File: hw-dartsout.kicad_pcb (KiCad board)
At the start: 2 copper layers, 45 parts, among them J1 Conn_01x10_Socket, J2 Conn_01x10_Socket, J3 Conn_01x02_Pin, J4 Conn_01x04_Pin, SW1 SW_Push, U1 ESP32-S3-WROOM-1, U3 NCP1117-3.3_SOT223

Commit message: PCB routed
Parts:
- removed TP2, TP3: TestPoint, TestPoint:TestPoint_Pad_D1.5mm
- added J5: Conn_01x10_Socket, Connector_PinSocket_2.54mm:PinSocket_1x10_P2.54mm_Vertical, F.Cu at (174.2, 118.6)
- added J6: Conn_01x10_Socket, Connector_PinSocket_2.54mm:PinSocket_1x10_P2.54mm_Vertical, F.Cu at (174.2, 103.5)
- added TP6: TestPoint, TestPoint:TestPoint_Pad_D1.5mm, F.Cu at (87.3, 96.8)
- H1, H2, H3, H4: footprint MountingHole:MountingHole_3.2mm_M3_Pad_TopBottom -> MountingHole:MountingHole_3.2mm_M3_DIN965_Pad_TopBottom
- U1: value ESP32-S3-WROOM-1 -> ESP32-S2-SOLO; footprint PCM_Espressif:ESP32-S3-WROOM-1 -> PCM_Espressif:ESP32-S2-SOLO
- moved H2 24.8 mm to (174.0, 98.1)
- moved H4 24.2 mm to (174.0, 126.9)
- moved JP1 15.8 mm to (164.4, 127.2), turned to 0 degrees
- moved JP2 14.5 mm to (153.8, 127.1), turned to 180 degrees
- moved TP4 8.96 mm to (94.9, 96.8), turned to 180 degrees
- moved TP5 7.72 mm to (98.7, 96.8), turned to 180 degrees
- moved TP1 5.16 mm to (91.1, 96.8), turned to 180 degrees
- moved H1 2.86 mm to (80.2, 98.1)
- moved H3 2.10 mm to (80.2, 126.9)
- moved J3 0.55 mm to (80.3, 110.1)
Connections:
- TP1 pad 1: Net-(U1-SPIIO6/GPIO35/FSPID/SUBSPID) -> Net-(U1-GPIO1/TOUCH1/ADC1_CH0)
- TP4 pad 1: Net-(U1-GPIO45) -> Net-(U1-GPIO2/TOUCH2/ADC1_CH1)
- U1 pad 10: /COL_05 -> /ROW_06
- U1 pad 11: /COL_06 -> /ROW_05
- U1 pad 12: /ROW_08 -> /ROW_04
- U1 pad 17: /ROW_09 -> /ROW_02
- U1 pad 18: /ROW_10 -> /ROW_01
- U1 pad 19: /COL_01 -> /COL_10
- U1 pad 20: /COL_02 -> /COL_09
- U1 pad 21: /COL_03 -> /COL_08
- U1 pad 22: /COL_04 -> /COL_07
- U1 pad 23: /COL_07 -> /COL_06
- U1 pad 24: /COL_09 -> /COL_05
- U1 pad 25: /COL_10 -> /COL_04
- U1 pad 26: Net-(U1-GPIO45) -> unconnected-(U1-GPIO45-Pad26)
- U1 pad 28: Net-(U1-SPIIO6/GPIO35/FSPID/SUBSPID) -> /COL_03
- U1 pad 29: Net-(U1-SPIIO7/GPIO36/FSPICLK/SUBSPICLK) -> /COL_02
- U1 pad 30: Net-(U1-SPIDQS/GPIO37/FSPIQ/SUBSPIQ) -> /COL_01
- U1 pad 31: /COL_08 -> Net-(U1-GPIO38/FSPIWP)
- U1 pad 38: /ROW_02 -> Net-(U1-GPIO2/TOUCH2/ADC1_CH1)
- U1 pad 39: /ROW_01 -> Net-(U1-GPIO1/TOUCH1/ADC1_CH0)
- U1 pad 4: /ROW_04 -> /ROW_10
- U1 pad 5: /ROW_05 -> /ROW_09
- U1 pad 6: /ROW_06 -> /ROW_08
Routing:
- net +3V3: track 0.00 -> 131.8 mm, vias 0 -> 2
- net /COL_03: track 31.5 -> 94.4 mm, vias 0 -> 3
- net /COL_02: track 34.0 -> 96.7 mm, vias 0 -> 3
- net /COL_01: track 36.6 -> 99.0 mm, vias 0 -> 3
- net /COL_04: track 28.9 -> 86.5 mm, vias 0 -> 1
- net /ROW_01: track 35.4 -> 91.6 mm
- net /ROW_02: track 31.6 -> 87.4 mm
- net /COL_05: track 26.4 -> 82.1 mm, vias 0 -> 1
- net /COL_06: track 23.9 -> 78.0 mm, vias 0 -> 1
- net /COL_07: track 21.3 -> 73.8 mm, vias 0 -> 1
- net /ROW_03: track 29.0 -> 80.7 mm
- net /COL_08: track 18.8 -> 69.6 mm, vias 0 -> 1
- net /COL_09: track 16.2 -> 65.4 mm, vias 0 -> 1
- net /ROW_04: track 27.0 -> 73.3 mm
- net /ROW_10: track 15.5 -> 60.8 mm
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- added copper zone on B.Cu, net GND
- added copper zone on F.Cu, net GND
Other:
- board outline added: 100 x 35 mm
- board text added: "+5V GND"
- board text added: "-MAY 2024-"
- board text added: "Dartsout"
- board text added: "GND RXD TXD 3V3"
- board text added: "Guille González"
- board text added: "PD PU"
- board text added: "PU PD"
- board text added: "Rev 0.1"

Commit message: Finish route, serigrphy and checks
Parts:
- removed TP5, TP6: TestPoint, TestPoint:TestPoint_Pad_D1.5mm
- removed U3: NCP1117-3.3_SOT223, Package_TO_SOT_SMD:SOT-223-3_TabPin2
- added D1: LED, LED_SMD:LED_0603_1608Metric, F.Cu at (85.7, 125.4)
- added D2: LED, LED_SMD:LED_0603_1608Metric, F.Cu at (92.2, 101.7)
- added D3: LED, LED_SMD:LED_0603_1608Metric, F.Cu at (92.2, 99.9)
- added R23: 1k, Resistor_SMD:R_0603_1608Metric, F.Cu at (85.7, 128.4)
- added R24: 1k, Resistor_SMD:R_0603_1608Metric, F.Cu at (95.3, 101.7)
- added R25: 1k, Resistor_SMD:R_0603_1608Metric, F.Cu at (95.3, 99.9)
- added TP2: TestPoint, TestPoint:TestPoint_Pad_D1.5mm, F.Cu at (90.2, 96.8)
- added TP3: TestPoint, TestPoint:TestPoint_Pad_D1.5mm, F.Cu at (86.3, 96.8)
- added U2: NCP1117-3.3_SOT223, Package_TO_SOT_SMD:SOT-223-3_TabPin2, F.Cu at (82.3, 116.7)
- C3: value 22u -> 100n; footprint Capacitor_SMD:C_0805_2012Metric -> Capacitor_SMD:C_0603_1608Metric
- C4: value 100n -> 22u; footprint Capacitor_SMD:C_0603_1608Metric -> Capacitor_SMD:C_0805_2012Metric
- R1, R10, R11, R12, R13, R14, R15, R16, R17, R18, R19, R2, R20, R3, R4, R5, R6, R7, R8, R9: value R -> 10k
- moved TP1 6.68 mm to (97.8, 96.8)
- moved J1 2.86 mm to (141.2, 118.6)
- moved J2 2.86 mm to (141.2, 103.5)
- moved R14 2.86 mm to (133.6, 110.5)
- moved R15 2.86 mm to (131.1, 110.5)
- moved R4 2.86 mm to (133.6, 126.6)
- moved R5 2.86 mm to (131.1, 126.6)
- moved R17 2.86 mm to (126.0, 110.5)
- moved R19 2.86 mm to (120.9, 110.5)
- moved R7 2.86 mm to (126.0, 126.6)
- moved R9 2.86 mm to (120.9, 126.6)
- moved R1 2.85 mm to (141.2, 126.6)
- moved R10 2.85 mm to (118.4, 126.6)
- moved R11 2.85 mm to (141.2, 110.5)
- moved R12 2.85 mm to (138.7, 110.5)
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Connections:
- net Net-(U1-GPIO2/TOUCH2/ADC1_CH1) renamed /LED2
- TP1 pad 1: Net-(U1-GPIO1/TOUCH1/ADC1_CH0) -> Net-(U1-GPIO46)
- U1 pad 39: Net-(U1-GPIO1/TOUCH1/ADC1_CH0) -> /LED1
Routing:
- net /LED1: track 0.00 -> 32.4 mm, vias 0 -> 2
- net Net-(U1-GPIO1/TOUCH1/ADC1_CH0): track 27.1 -> 0.00 mm, vias 2 -> 0
- net /LED2: track 27.2 -> 31.3 mm
- net /ROW_01: track 91.6 -> 95.6 mm
- net /ROW_02: track 87.4 -> 91.5 mm
- net /ROW_03: track 80.7 -> 84.8 mm
- net Net-(D1-K): track 0.00 -> 3.01 mm
- net /ROW_06: track 67.2 -> 69.8 mm
- net /ROW_05: track 70.2 -> 72.8 mm
- net /ROW_04: track 73.3 -> 75.9 mm
- net /ROW_07: track 63.3 -> 65.4 mm
- net /ROW_COM: track 45.6 -> 47.5 mm
- net /COL_08: track 69.6 -> 71.5 mm
- net /COL_09: track 65.4 -> 67.2 mm
- net /COL_01: track 99.0 -> 100.9 mm
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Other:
- outline, holes or cut-outs redrawn
- board text added: "MAY 2024"

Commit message: Revision 0.1
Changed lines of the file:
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@@
       (plot_on_all_layers_selection 0x0000000_00000000)
       (disableapertmacros false)
-      (usegerberextensions false)
-      (usegerberattributes true)
-      (usegerberadvancedattributes true)
-      (creategerberjobfile true)
+      (usegerberextensions true)
+      (usegerberattributes false)
+      (usegerberadvancedattributes false)
+      (creategerberjobfile false)
       (dashed_line_dash_ratio 12.000000)
       (dashed_line_gap_ratio 3.000000)
@@
       (psa4output false)
       (plotreference true)
-      (plotvalue true)
+      (plotvalue false)
       (plotinvisibletext false)
       (sketchpadsonfab false)
-      (subtractmaskfromsilk false)
+      (subtractmaskfromsilk true)
       (outputformat 1)
       (mirror false)
-      (drillshape 1)
+      (drillshape 0)
       (scaleselection 1)
-      (outputdirectory "")
+      (outputdirectory "outputs/gerbers/")
     )
   )
@@
     (property "ki_keywords" "esp32-s2 solo")
     (attr smd)
-    (fp_text reference "U1" (at 0 -17.05 180) (layer "F.SilkS")
+    (fp_text reference "U1" (at -8.7 11.275 180) (layer "F.SilkS")
         (effects (font (size 1 1) (thickness 0.15)))
     )
@@
     (property "ki_keywords" "cap capacitor")
     (attr smd)
-    (fp_text reference "C4" (at 2.6 0) (layer "F.SilkS")
+    (fp_text reference "C4" (at -0.075 3.375) (layer "F.SilkS")
         (effects (font (size 1 1) (thickness 0.15)))
     )
@@
     (property "ki_keywords" "cap capacitor")
     (attr smd)
-    (fp_text reference "C3" (at 2.475 0.025) (layer "F.SilkS")
-        (effects (font (size 1 1) (thickness 0.15)))
-    )
+    (fp_text reference "C3" (at -0.025 3.775) (layer "F.SilkS")
+        (effects (font (size 1 1) (thickness 0.15)))
+    )

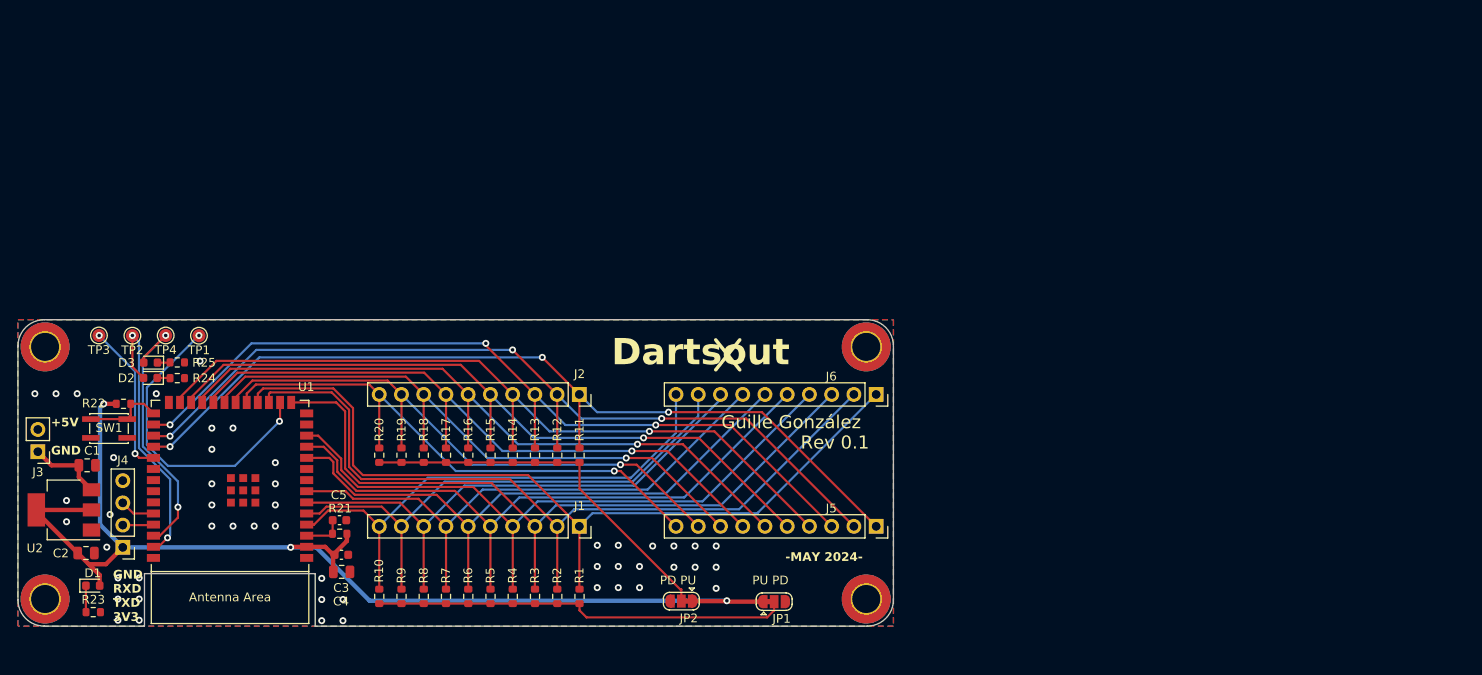
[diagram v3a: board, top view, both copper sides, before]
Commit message: Changed sch and start with layout for next version
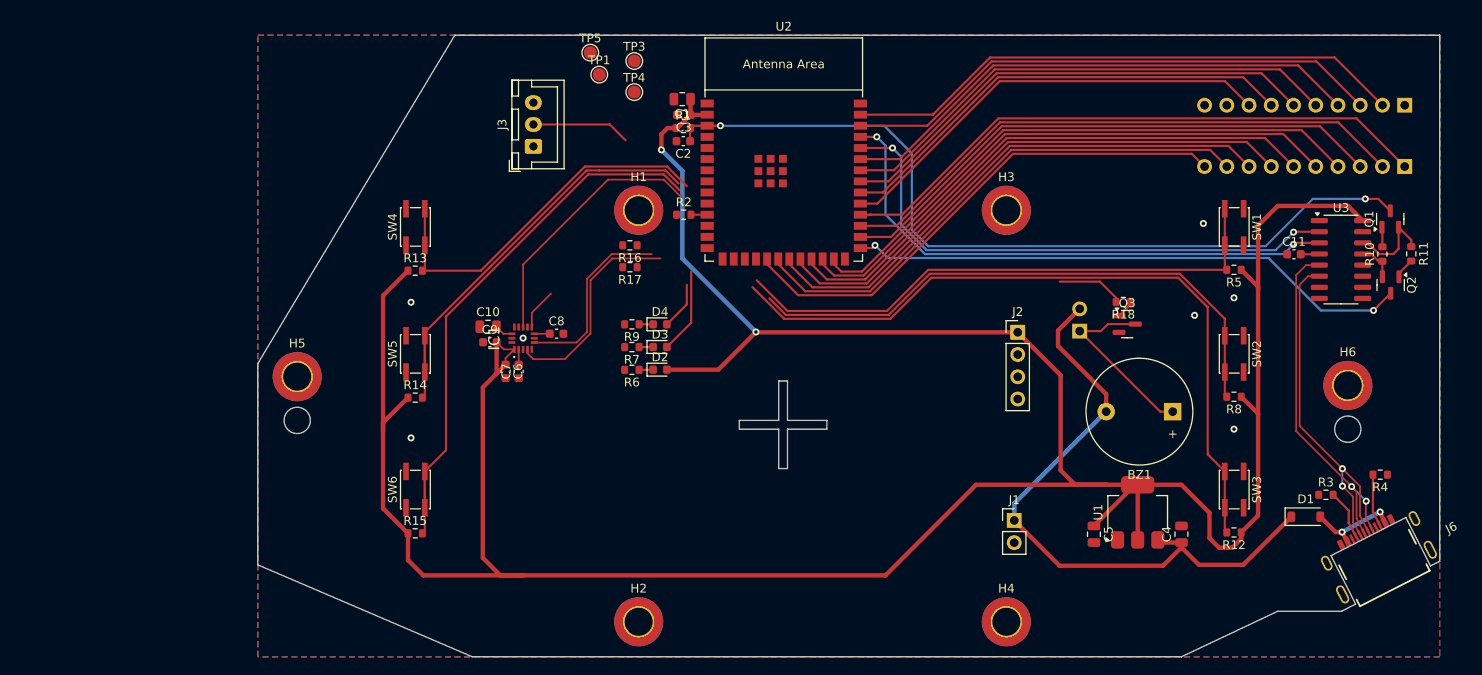
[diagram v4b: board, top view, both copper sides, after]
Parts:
- removed JP1, JP2: SolderJumper_3_Bridged12, Jumper:SolderJumper-3_P1.3mm_Bridged12_RoundedPad1.0x1.5mm
- removed R19, R20, R21, R22: 10k, Resistor_SMD:R_0603_1608Metric
- removed R23, R24, R25: 1k, Resistor_SMD:R_0603_1608Metric
- removed TP2: TestPoint, TestPoint:TestPoint_Pad_D1.5mm
- added BZ1: Buzzer, Buzzer_Beeper:Buzzer_12x9.5RM7.6, F.Cu at (209.0, 105.5)
- added C10: 4u7, Capacitor_SMD:C_0805_2012Metric, F.Cu at (130.8, 95.8)
- added C11: 100n, Capacitor_SMD:C_0603_1608Metric, F.Cu at (222.8, 87.5)
- added C6: 100n, Capacitor_SMD:C_0603_1608Metric, F.Cu at (132.8, 100.9)
- added C7: 100n, Capacitor_SMD:C_0603_1608Metric, F.Cu at (134.3, 100.9)
- added C8: 100n, Capacitor_SMD:C_0603_1608Metric, F.Cu at (138.6, 96.6)
- added C9: 100n, Capacitor_SMD:C_0603_1608Metric, F.Cu at (131.0, 97.6)
- added D4: LED, LED_SMD:LED_0603_1608Metric, F.Cu at (150.4, 95.5)
- added H5: MountingHole_Pad, MountingHole:MountingHole_3.2mm_M3_DIN965_Pad_TopBottom, F.Cu at (109.0, 101.5)
- added H6: MountingHole_Pad, MountingHole:MountingHole_3.2mm_M3_DIN965_Pad_TopBottom, F.Cu at (229.0, 102.5)
- added IC1: FXOS8700CQ, guille-lib:FXOS8700CQ, F.Cu at (134.8, 97.1)
- added J7: Conn_01x02_Pin, Connector_PinHeader_2.54mm:PinHeader_1x02_P2.54mm_Horizontal, B.Cu at (198.4, 96.3)
- added Q1: PMBT3904235, Package_TO_SOT_SMD:SOT-23, F.Cu at (233.8, 83.5)
- added Q2: PMBT3904235, Package_TO_SOT_SMD:SOT-23, F.Cu at (233.9, 91.0)
- added Q3: PMBT3904235, Package_TO_SOT_SMD:SOT-23, F.Cu at (203.8, 95.5)
- added SW2: SW_Push, guille-lib:SW_SPST_PTS810, F.Cu at (216.0, 98.9)
- added SW3: SW_Push, guille-lib:SW_SPST_PTS810, F.Cu at (216.0, 114.4)
- added SW4: SW_Push, guille-lib:SW_SPST_PTS810, F.Cu at (122.5, 84.4)
- added SW5: SW_Push, guille-lib:SW_SPST_PTS810, F.Cu at (122.5, 98.9)
- added SW6: SW_Push, guille-lib:SW_SPST_PTS810, F.Cu at (122.5, 114.4)
- added TP5: TestPoint, TestPoint:TestPoint_Pad_D1.5mm, F.Cu at (142.5, 64.5)
- added U3: CH340C, Package_SO:SOIC-16_3.9x9.9mm_P1.27mm, F.Cu at (228.2, 88.1)
- C1: value 10u -> 22u
- C2: value 10u -> 1u; footprint Capacitor_SMD:C_0805_2012Metric -> Capacitor_SMD:C_0603_1608Metric
- C4: value 22u -> 10u
- C5: value 1u -> 10u; footprint Capacitor_SMD:C_0603_1608Metric -> Capacitor_SMD:C_0805_2012Metric
- D1: value LED -> 1N4448W-7-F; footprint LED_SMD:LED_0603_1608Metric -> Diode_SMD:D_SOD-123
- J1: value Conn_01x10_Socket -> Conn_01x02_Pin; footprint Connector_PinSocket_2.54mm:PinSocket_1x10_P2.54mm_Vertical -> Connector_PinHeader_2.54mm:PinHeader_1x02_P2.54mm_Vertical
- J2: value Conn_01x10_Socket -> Conn_01x04_Pin; footprint Connector_PinSocket_2.54mm:PinSocket_1x10_P2.54mm_Vertical -> Connector_PinHeader_2.54mm:PinHeader_1x04_P2.54mm_Vertical
- J3: value Conn_01x02_Pin -> Conn_01x03_Pin; footprint Connector_PinHeader_2.54mm:PinHeader_1x02_P2.54mm_Vertical -> Connector_JST:JST_XH_B3B-XH-A_1x03_P2.50mm_Vertical
- J4: value Conn_01x04_Pin -> Conn_01x10_Socket; footprint Connector_PinHeader_2.54mm:PinHeader_1x04_P2.54mm_Vertical -> Connector_PinSocket_2.54mm:PinSocket_1x10_P2.54mm_Vertical; moved to B.Cu
- J5: moved to B.Cu
- J6: value Conn_01x10_Socket -> USB4510-03-1-A; footprint Connector_PinSocket_2.54mm:PinSocket_1x10_P2.54mm_Vertical -> guille-lib:USB4510031A
- R16, R17, R18, R6, R7, R9: value 10k -> 1k
- R3, R4: value 10k -> 5k1
- U1: value ESP32-S2-SOLO -> NCP1117-3.3_SOT223; footprint PCM_Espressif:ESP32-S2-SOLO -> Package_TO_SOT_SMD:SOT-223-3_TabPin2
- U2: value NCP1117-3.3_SOT223 -> ESP32-S2-SOLO; footprint Package_TO_SOT_SMD:SOT-223-3_TabPin2 -> guille-lib:ESP32-S2-SOLO
- moved J4 154.9 mm to (235.5, 70.5), turned to 90 degrees
- moved D1 138.8 mm to (224.2, 117.5)
- moved SW1 130.6 mm to (216.0, 84.4), turned to -90 degrees
- moved R10 121.1 mm to (232.9, 87.5)
- moved H3 118.4 mm to (190.0, 82.5)
- moved U1 103.7 mm to (205.0, 117.0), turned to 90 degrees
- moved R4 100.1 mm to (232.7, 112.7), turned to 180 degrees
- moved R11 97.7 mm to (236.2, 87.5), turned to -90 degrees
- moved C4 96.0 mm to (210.0, 119.5), turned to 90 degrees
- moved R8 95.3 mm to (216.0, 103.8), turned to 180 degrees
- moved R5 92.8 mm to (216.0, 89.3), turned to 180 degrees
- moved R3 91.1 mm to (226.5, 115.0), turned to 0 degrees
- moved U2 90.6 mm to (164.6, 78.6), turned to 0 degrees
- moved C5 86.2 mm to (200.0, 119.5), turned to -90 degrees
- moved C2 82.9 mm to (153.1, 74.6), turned to 180 degrees
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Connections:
- C1 pad 1: +5V -> +3V3
- C2 pad 1: +3V3 -> /ESP_EN
- C4 pad 1: +3V3 -> +5V
- C5 pad 1: Net-(U1-EN) -> +3V3
- D1 pad 1: Net-(D1-K) -> +5V
- D1 pad 2: +3V3 -> VBUS
- D2 pad 2: /LED1 -> +3V3
- D3 pad 2: /LED2 -> /LED1
- J1 pad 1: /ROW_01 -> +5V
- J1 pad 2: /ROW_02 -> GND
- J2 pad 1: /COL_01 -> +3V3
- J2 pad 2: /COL_02 -> /ESP_TX
- J2 pad 3: /COL_03 -> /ESP_RX
- J2 pad 4: /COL_04 -> GND
- J3 pad 1: +5V -> GND
- J3 pad 2: GND -> /LEDS_DATA
- J4 pad 1: +3V3 -> unconnected-(J4-Pin_1-Pad1)
- J4 pad 2: /ESP_TX -> /ROW_01
- J4 pad 3: /ESP_RX -> /ROW_02
- J4 pad 4: GND -> /ROW_03
- R1 pad 1: /ROW_COM -> +3V3
- R1 pad 2: /ROW_01 -> /ESP_EN
- R10 pad 1: /ROW_COM -> Net-(U3-~{DTR})
- R10 pad 2: /ROW_10 -> Net-(Q1-Pad1)
- R11 pad 1: /COL_COM -> Net-(U3-~{RTS})
- R11 pad 2: /COL_01 -> Net-(Q2-Pad1)
- R12 pad 1: /COL_COM -> +3V3
- R12 pad 2: /COL_02 -> /BTN3
- R13 pad 1: /COL_COM -> +3V3
- R13 pad 2: /COL_03 -> /BTN4
- R14 pad 1: /COL_COM -> +3V3
- R14 pad 2: /COL_04 -> /BTN5
- R15 pad 1: /COL_COM -> +3V3
- R15 pad 2: /COL_05 -> /BTN6
- R16 pad 1: /COL_COM -> +3V3
- R16 pad 2: /COL_06 -> /I2C_SDA
- R17 pad 1: /COL_COM -> +3V3
- R17 pad 2: /COL_07 -> /I2C_SCL
- R18 pad 1: /COL_COM -> Net-(Q3-Pad1)
- R18 pad 2: /COL_08 -> /SPEAKER
- R2 pad 1: /ROW_COM -> +3V3
- R2 pad 2: /ROW_02 -> Net-(U2-GPIO18/U1RXD/ADC2_CH7/DAC_2/CLK_OUT3)
- R3 pad 1: /ROW_COM -> GND
- R3 pad 2: /ROW_03 -> Net-(J6-CC1)
- R4 pad 1: /ROW_COM -> GND
- R4 pad 2: /ROW_04 -> Net-(J6-CC2)
- R5 pad 1: /ROW_COM -> +3V3
- R5 pad 2: /ROW_05 -> /BTN1
- R6 pad 1: /ROW_COM -> Net-(D2-K)
- R6 pad 2: /ROW_06 -> GND
- R7 pad 1: /ROW_COM -> Net-(D3-K)
- R7 pad 2: /ROW_07 -> GND
- R8 pad 1: /ROW_COM -> +3V3
- R8 pad 2: /ROW_08 -> /BTN2
- R9 pad 1: /ROW_COM -> Net-(D4-K)
- R9 pad 2: /ROW_09 -> GND
- SW1 pad 2: /ESP_IO0 -> /BTN1
- TP1 pad 1: Net-(U1-GPIO46) -> Net-(U2-GPIO46)
- TP3 pad 1: Net-(U1-GPIO38/FSPIWP) -> /LEDS_DATA
- TP4 pad 1: /LED2 -> Net-(U2-GPIO45)
- U1 pad 3: Net-(U1-EN) -> +5V
- U2 pad 3: +5V -> /ESP_EN
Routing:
- net +3V3: track 131.7 -> 354.7 mm, vias 3 -> 2
- net /ESP_EN: track 0.00 -> 95.2 mm, vias 0 -> 2
- net /BTN3: track 0.00 -> 83.5 mm
- net /BTN2: track 0.00 -> 65.9 mm
- net /BTN1: track 0.00 -> 64.4 mm
- net +5V: track 8.72 -> 73.0 mm
- net /BTN6: track 0.00 -> 64.2 mm
- net /ROW_08: track 62.2 -> 0.00 mm
- net /ROW_09: track 61.5 -> 0.00 mm
- net /ESP_TX: track 3.52 -> 63.1 mm, vias 0 -> 2
- net /ROW_10: track 59.6 -> 0.00 mm
- net /ESP_RX: track 4.23 -> 62.7 mm, vias 0 -> 2
- net /ESP_IO0: track 9.11 -> 64.6 mm, vias 0 -> 2
- net /BTN5: track 0.00 -> 49.2 mm
- net /ROW_COM: track 47.5 -> 0.00 mm
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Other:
- board size 100 x 35 mm -> 135 x 71 mm
- board text removed: "+5V GND"
- board text removed: "-MAY 2024-"
- board text removed: "Dartsout"
- board text removed: "GND RXD TXD 3V3"
- board text removed: "Guille González"
- board text removed: "MAY 2024"
- board text removed: "PD PU"
- board text removed: "PU PD"
- board text removed: "Rev 0.1"

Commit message: Add changes for revision 0.2
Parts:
- removed R2: 10k, Resistor_SMD:R_0603_1608Metric
- added TP2: TestPoint, TestPoint:TestPoint_Pad_D1.5mm, F.Cu at (138.1, 92.5)
- moved TP4 42.4 mm to (182.1, 93.5)
- moved TP1 28.6 mm to (156.6, 92.4)
- moved TP3 19.7 mm to (141.3, 84.1)
- moved TP5 19.6 mm to (153.0, 81.0)
- moved D4 6.48 mm to (150.5, 102.0)
- moved R9 6.48 mm to (147.3, 102.0)
- moved D2 4.81 mm to (150.5, 95.9)
- moved R6 4.81 mm to (147.3, 95.9)
- moved C1 1.69 mm to (152.0, 68.4)
- moved C2 1.69 mm to (152.1, 73.2)
- moved C3 1.69 mm to (152.2, 70.2)
- moved R1 1.69 mm to (152.1, 71.7)
- moved R17 1.41 mm to (146.7, 90.4)
- moved R7 0.89 mm to (147.3, 99.0)
- moved D3 0.89 mm to (150.5, 99.0)
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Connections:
- TP3 pad 1: /LEDS_DATA -> /FXOS_INT1
- U2 pad 11: Net-(U2-GPIO18/U1RXD/ADC2_CH7/DAC_2/CLK_OUT3) -> /I2C_SDA
- U2 pad 12: /BTN4 -> /I2C_SCL
- U2 pad 13: /LED2 -> /LED1
- U2 pad 14: /LED1 -> /LED2
- U2 pad 15: unconnected-(U2-GPIO3/TOUCH3/ADC1_CH2-Pad15) -> /BTN3
- U2 pad 17: /BTN5 -> /BTN2
- U2 pad 18: /BTN6 -> /BTN1
- U2 pad 4: unconnected-(U2-GPIO4/TOUCH4/ADC1_CH3-Pad4) -> /LEDS_DATA
- U2 pad 5: /BTN1 -> /BTN4
- U2 pad 6: /BTN2 -> /BTN5
- U2 pad 7: /BTN3 -> /BTN6
- U2 pad 8: /LEDS_DATA -> /FXOS_INT1
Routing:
- net +5V: track 73.0 -> 213.0 mm, vias 0 -> 1
- net /SPEAKER: track 7.68 -> 51.4 mm, vias 0 -> 2
- net GND: track 0.00 -> 21.1 mm, vias 7 -> 176
- net Net-(U2-GPIO45): track 0.00 -> 19.3 mm, vias 0 -> 2
- net /ESP_RX: track 62.7 -> 78.3 mm, vias 2 -> 3
- net /ESP_TX: track 63.1 -> 75.6 mm, vias 2 -> 3
- net /LED2: track 5.47 -> 17.1 mm
- net +3V3: track 354.7 -> 364.2 mm, vias 2 -> 4
- net /I2C_SDA: track 21.2 -> 30.6 mm
- net /LEDS_DATA: track 11.3 -> 20.4 mm
- net Net-(U2-GPIO46): track 0.00 -> 9.06 mm, vias 0 -> 2
- net /I2C_SCL: track 24.2 -> 32.4 mm
- net /BTN2: track 65.9 -> 73.6 mm
- net /BTN3: track 83.5 -> 90.4 mm
- net /LED1: track 9.76 -> 15.9 mm
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- added copper zone on F.Cu, net +3V3
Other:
- outline, holes or cut-outs redrawn
- board text added: "+3V3 TX RX GND"
- board text added: "+5V BUZZ"
- board text added: "+5V DATA GND"
- board text added: "+5V GND"
- board text added: "Board ID: ______________________________"
- board text added: "C1 C2 C3 C4 C5 C6 C7 C8 C9 10"
- board text added: "DartsOut"
- board text added: "Guillermo González"
- board text added: "LED1"
- board text added: "LED2"
- board text added: "NOV 2024"
- board text added: "POWER"
- board text added: "R1 R2 R3 R4 R5 R6 R7"
- board text added: "Rev 0.2"
